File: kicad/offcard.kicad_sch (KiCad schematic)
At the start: 30 parts, among them J10 lower fan, J4 heater, J5 5kg load cell, J6 LCD, J7 upper fan, J8 motor, M1 12VDC motor, U2 IRLML2502TRPBF, U3 NAU7802SGI

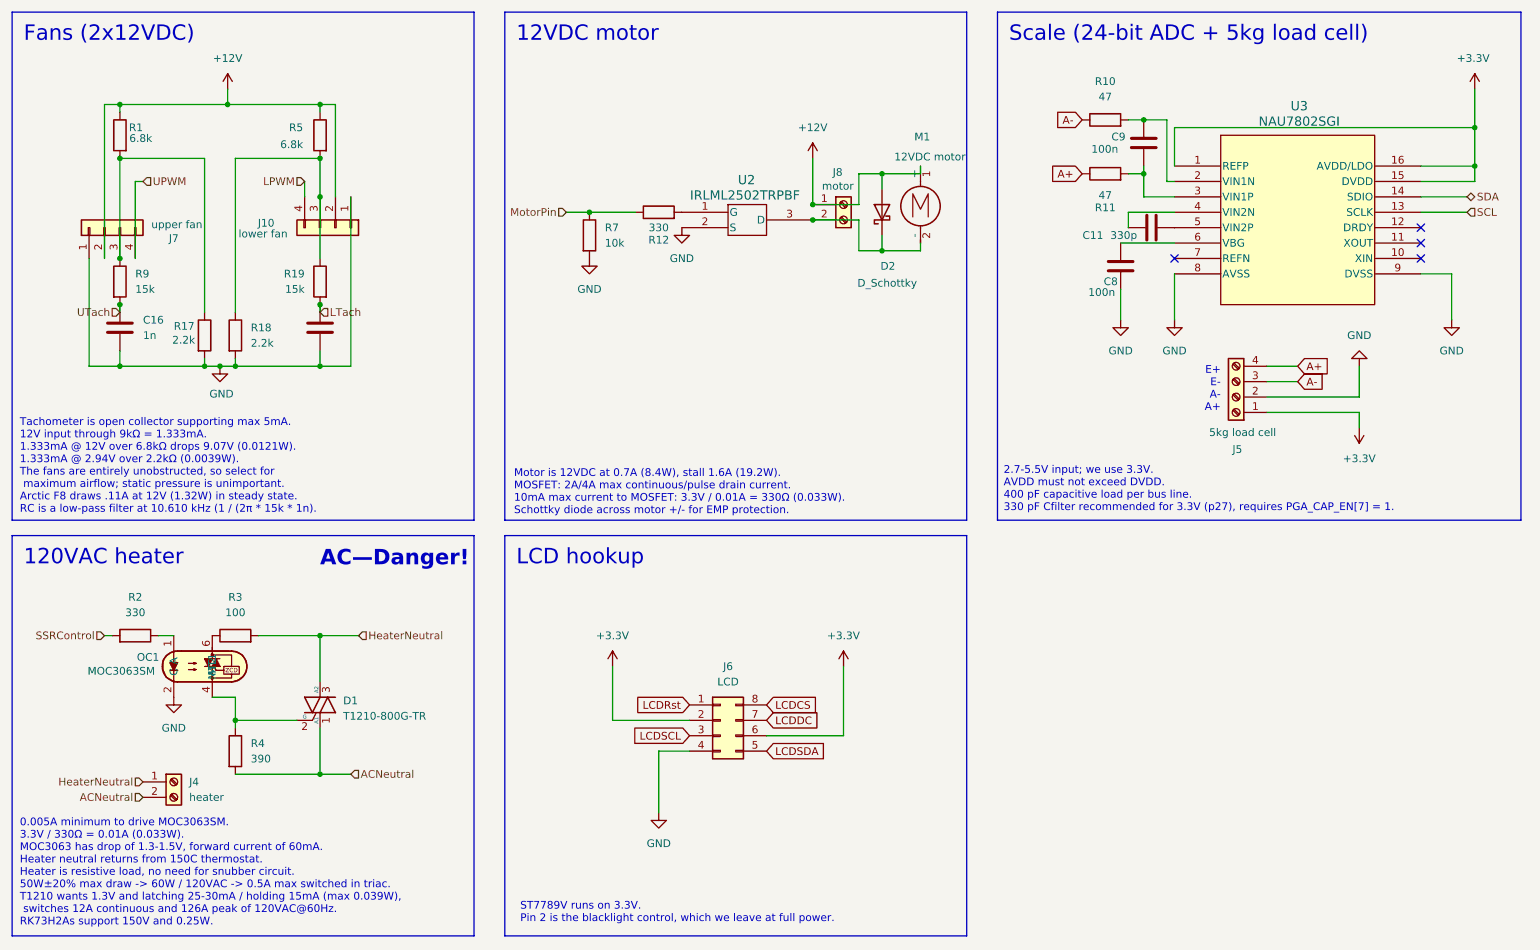
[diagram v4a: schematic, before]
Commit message: rotate MOSFET
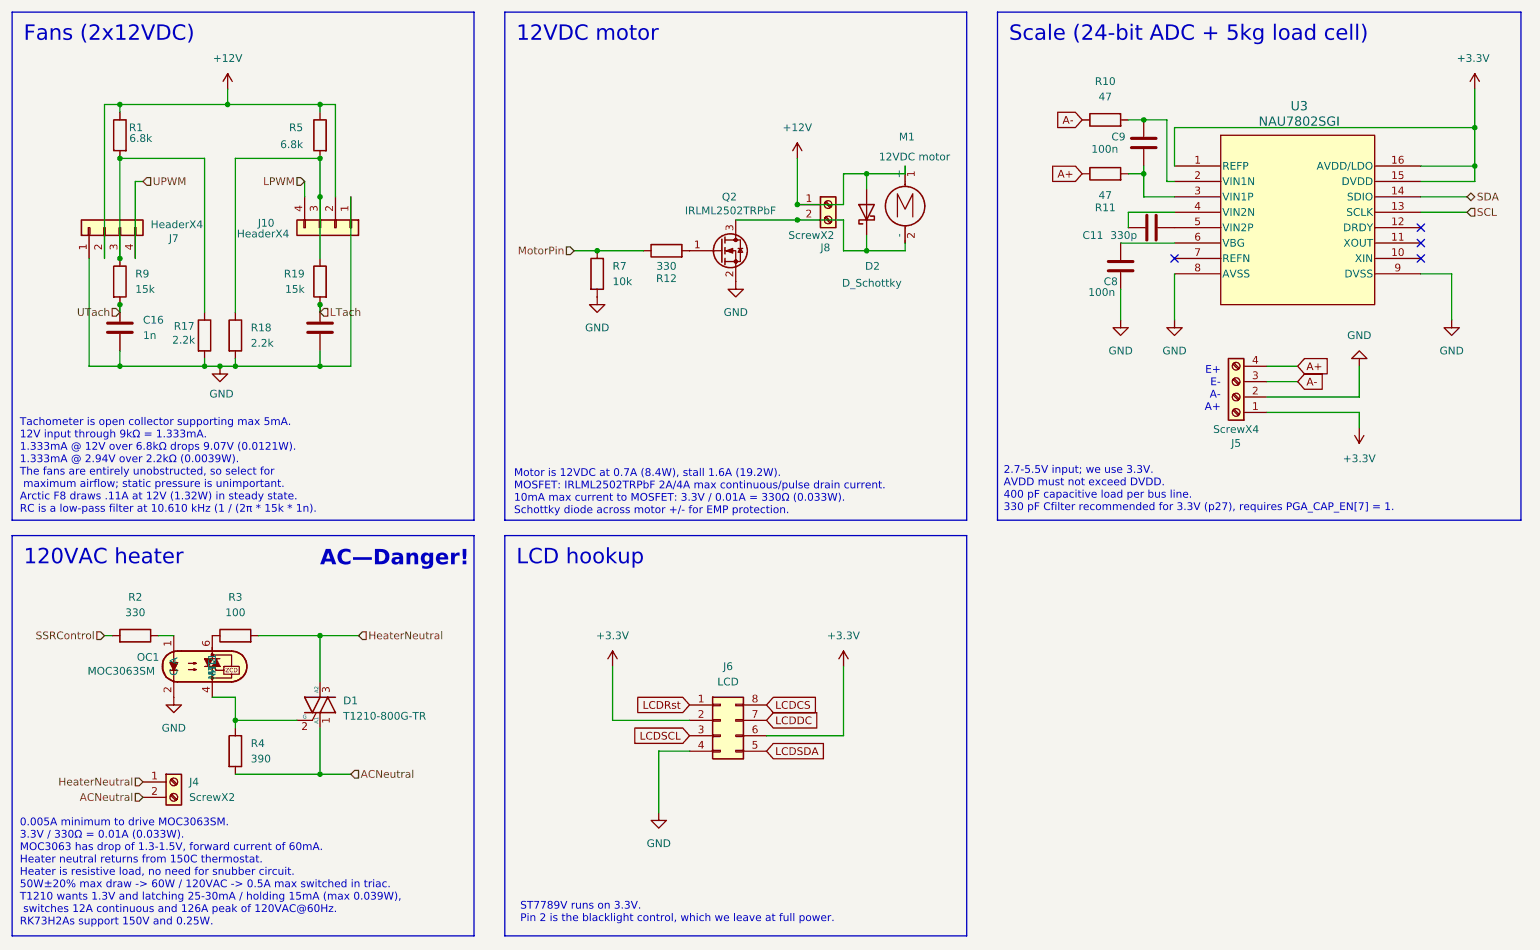
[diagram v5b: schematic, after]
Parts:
- removed U2: IRLML2502TRPBF, dank:IRLML2502TRPBF, symbol dank:IRLML2502TRPBF
- added Q2: IRLML2502TRPbF, dank:IRLML2502TRPBF, symbol Transistor_FET:Q_NMOS_GSD
- J10: value lower fan -> HeaderX4
- J4: value heater -> ScrewX2
- J5: value 5kg load cell -> ScrewX4
- J7: value upper fan -> HeaderX4
- J8: value motor -> ScrewX2
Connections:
- net GND: now also Q2.2 (S)
- net at D2.1 (K), J8.2 (Pin_2), M1.2 (-): now also Q2.3 (D)
- net at R12.2: now also Q2.1 (G)
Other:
- note added: "Motor is 12VDC at 0.7A (8.4W), stall 1.6A (19.2W). MOSFET: IRLML2502TRPbF 2A/4A max continuous/pulse drain current. 10mA max current to MOSFET: 3.3V / 0.01A = 330Ω (0.033W). Schottky diode across motor +/- for EMP protection."
- note removed: "Motor is 12VDC at 0.7A (8.4W), stall 1.6A (19.2W). MOSFET: 2A/4A max continuous/pulse drain current. 10mA max current to MOSFET: 3.3V / 0.01A = 330Ω (0.033W). Schottky diode across motor +/- for EMP protection."
- moved on the sheet: D2, J8, M1, R12, R7

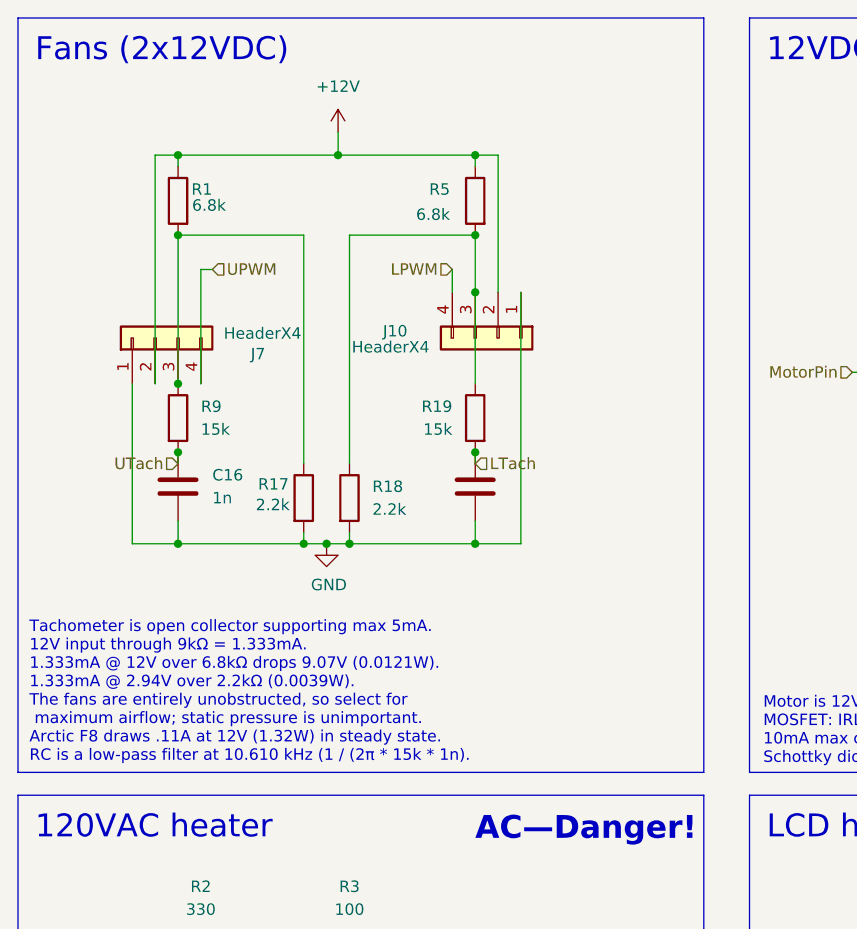
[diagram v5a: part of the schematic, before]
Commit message: elaborate layout changes to eliminate a voltage divider
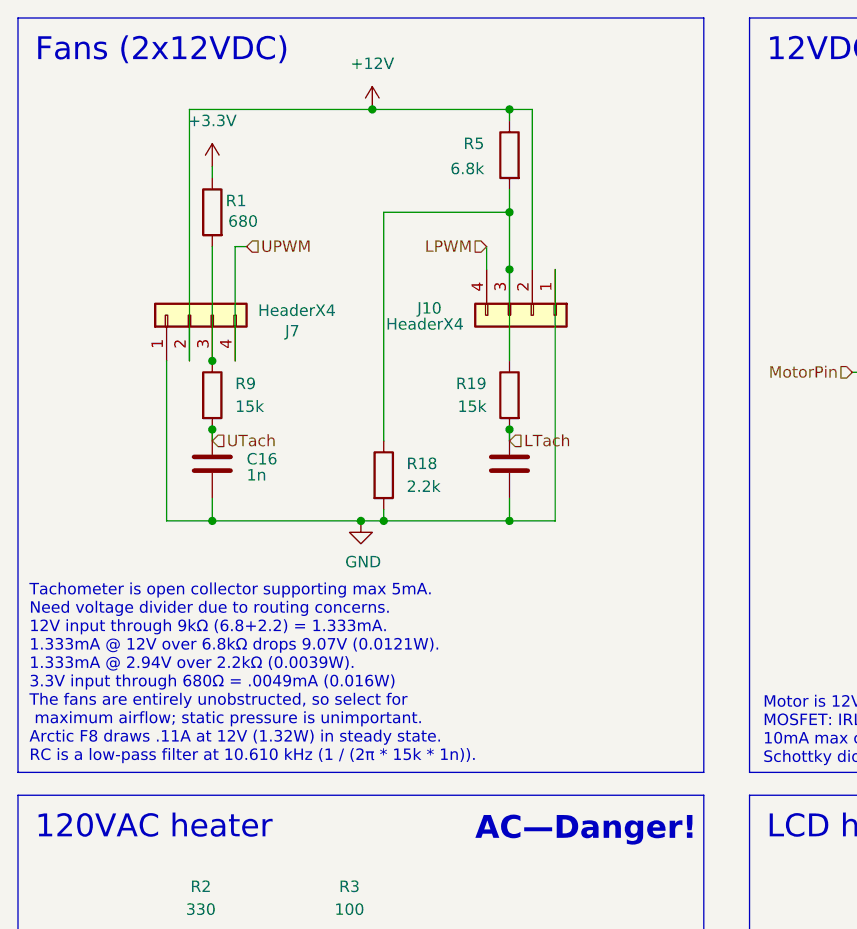
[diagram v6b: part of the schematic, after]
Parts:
- removed R17: 2.2k, Resistor_SMD:R_0805_2012Metric_Pad1.20x1.40mm_HandSolder, symbol Device:R
- C11, C15, C16, C8: footprint Capacitor_SMD:C_0805_2012Metric_Pad1.18x1.45mm_HandSolder -> Capacitor_SMD:C_1206_3216Metric_Pad1.33x1.80mm_HandSolder
- R1: value 6.8k -> 680
- R18, R19, R5, R9: footprint Resistor_SMD:R_0805_2012Metric_Pad1.20x1.40mm_HandSolder -> Resistor_SMD:R_1206_3216Metric_Pad1.30x1.75mm_HandSolder
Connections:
- net +12V: no longer R1.1
- net +3.3V: now also R1.1
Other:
- note added: "Tachometer is open collector supporting max 5mA. Need voltage divider due to routing concerns. 12V input through 9kΩ (6.8+2.2) = 1.333mA. 1.333mA @ 12V over 6.8kΩ drops 9.07V (0.0121W). 1.333mA @ 2.94V over 2.2kΩ (0.0039W). 3.3V input through 680Ω = .0049mA (0.016W) The fans are entirely unobstructed, so select for maximum airflow; static pressure is unimportant. Arctic F8 draws .11A at 12V (1.32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"
- note removed: "Tachometer is open collector supporting max 5mA. 12V input through 9kΩ = 1.333mA. 1.333mA @ 12V over 6.8kΩ drops 9.07V (0.0121W). 1.333mA @ 2.94V over 2.2kΩ (0.0039W). The fans are entirely unobstructed, so select for maximum airflow; static pressure is unimportant. Arctic F8 draws .11A at 12V (1.32W) in steady state. RC is a low-pass filter at 10.610 kHz (1 / (2π * 15k * 1n)."
- moved on the sheet: C16, J10, J7, R1, R18, R19, R5, R9

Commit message: v2.1.5
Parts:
- C9: footprint Capacitor_SMD:C_0805_2012Metric_Pad1.18x1.45mm_HandSolder -> Capacitor_SMD:C_1206_3216Metric_Pad1.33x1.80mm_HandSolder
- R1, R3, R4: footprint Resistor_SMD:R_0805_2012Metric_Pad1.20x1.40mm_HandSolder -> Resistor_SMD:R_1206_3216Metric_Pad1.30x1.75mm_HandSolder
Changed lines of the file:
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@@
 			)
 		)
-		(property "Footprint" "Resistor_SMD:R_0805_2012Metric_Pad1.20x1.40mm_HandSolder"
+		(property "Footprint" "Resistor_SMD:R_1206_3216Metric_Pad1.30x1.75mm_HandSolder"
 			(at 38.608 39.37 90)
 			(effects
@@
 			)
 		)
-		(property "Footprint" "Resistor_SMD:R_0805_2012Metric_Pad1.20x1.40mm_HandSolder"
+		(property "Footprint" "Resistor_SMD:R_1206_3216Metric_Pad1.30x1.75mm_HandSolder"
 			(at 50.292 139.7 90)
 			(effects
@@
 			)
 		)
-		(property "Footprint" "Resistor_SMD:R_0805_2012Metric_Pad1.20x1.40mm_HandSolder"
+		(property "Footprint" "Resistor_SMD:R_1206_3216Metric_Pad1.30x1.75mm_HandSolder"
 			(at 52.07 122.428 90)
 			(effects
@@
 			)
 		)
-		(property "Footprint" "Capacitor_SMD:C_0805_2012Metric_Pad1.18x1.45mm_HandSolder"
+		(property "Footprint" "Capacitor_SMD:C_1206_3216Metric_Pad1.33x1.80mm_HandSolder"
 			(at 202.8952 43.18 0)
 			(effects

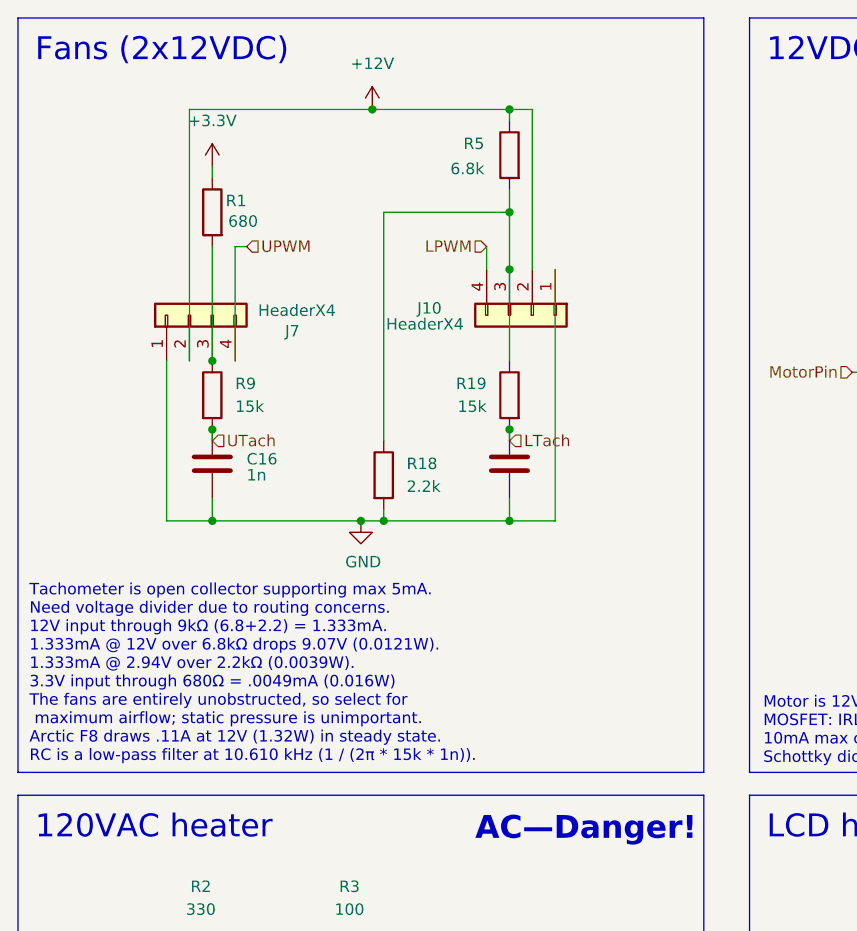
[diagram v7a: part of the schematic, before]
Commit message: kill RC low pass filter on tachometers
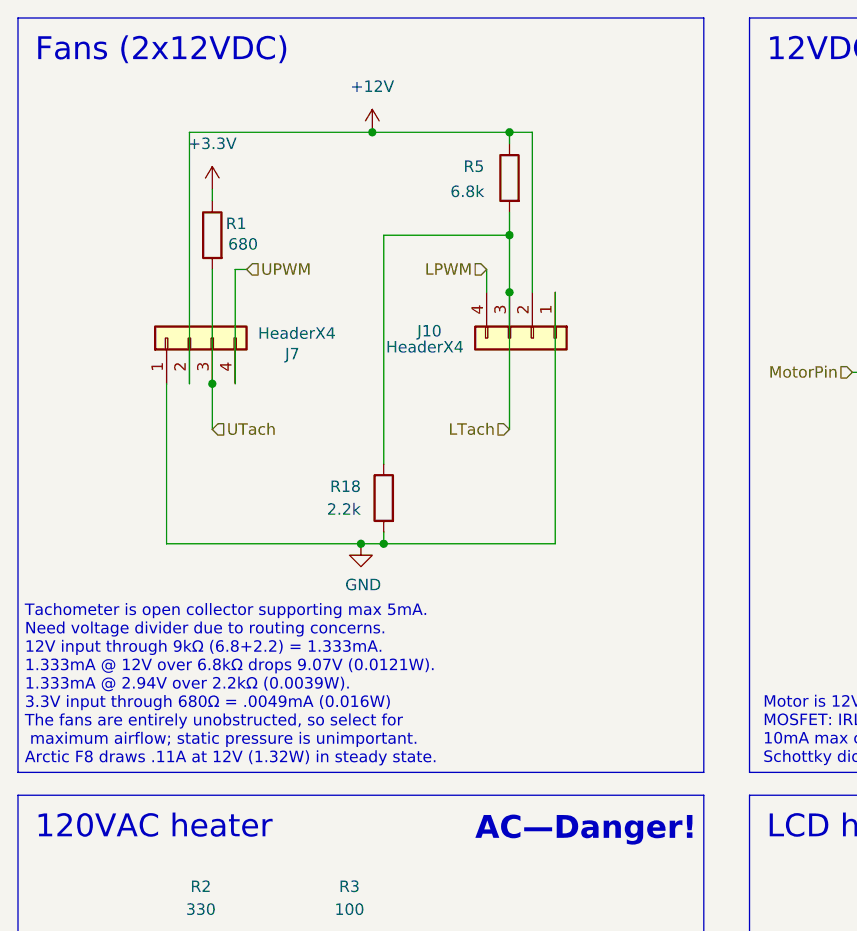
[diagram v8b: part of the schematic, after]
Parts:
- removed C15, C16: 1n, Capacitor_SMD:C_1206_3216Metric_Pad1.33x1.80mm_HandSolder, symbol Device:C
- removed R19, R9: 15k, Resistor_SMD:R_1206_3216Metric_Pad1.30x1.75mm_HandSolder, symbol Device:R
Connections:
- net LTach: now also J10.3 (Pin_3), R18.1, R5.2
- net UTach: now also J7.3 (Pin_3), R1.2
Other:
- moved on the sheet: J10, J7, R1, R18, R5
